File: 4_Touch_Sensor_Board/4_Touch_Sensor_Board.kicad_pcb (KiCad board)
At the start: 2 copper layers, 60 x 31 mm, 21 parts, among them J1 Conn_02x05, U1 TTP224B

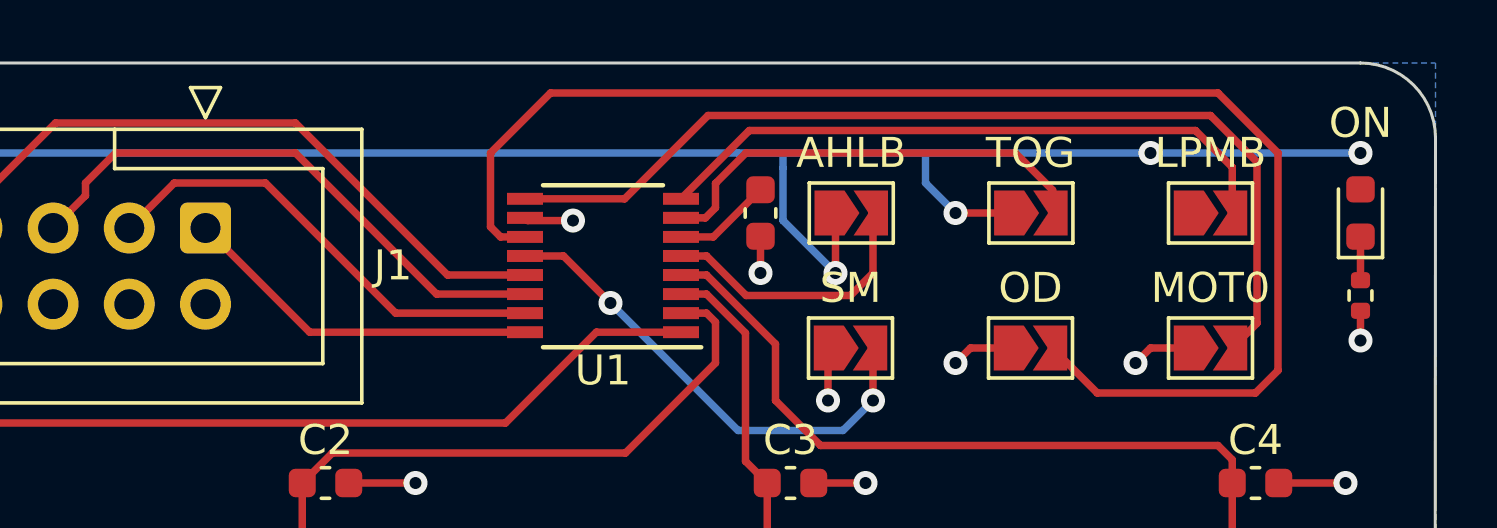
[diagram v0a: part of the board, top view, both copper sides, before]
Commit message: fix board file and add BOM an POS files to JLCPCB
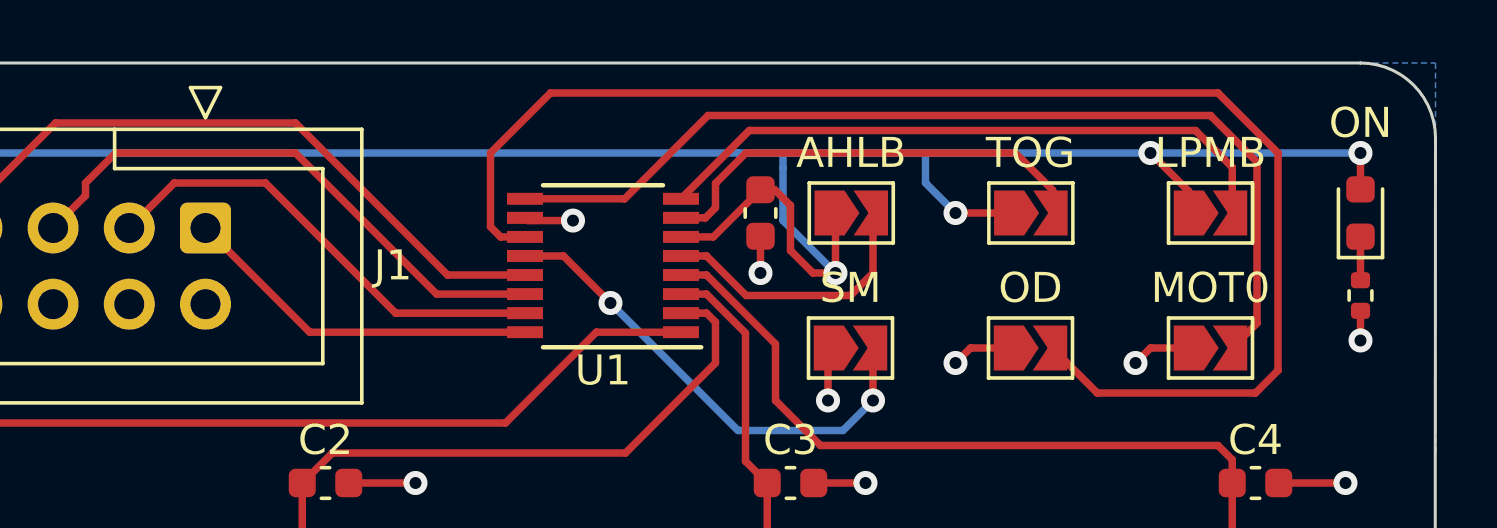
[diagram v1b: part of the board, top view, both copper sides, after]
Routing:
- net +3V3: track 64.0 -> 72.3 mm
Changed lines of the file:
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@@
       (outputformat 1)
       (mirror false)
-      (drillshape 1)
+      (drillshape 0)
       (scaleselection 1)
-      (outputdirectory "")
+      (outputdirectory "Fab/")
     )
   )
@@
     (fp_line (start -1.98 -3.91) (end 4.52 -3.91) (layer "F.Fab") (width 0.1))
     (fp_line (start -1.98 14.07) (end -1.98 7.13) (layer "F.Fab") (width 0.1))
-    (pad "1" thru_hole roundrect locked (at 0 0 270) (size 1.7 1.7) (drill 1) (layers *.Cu *.Mask) (roundrect_rratio 0.147059)
+    (pad "1" thru_hole roundrect locked (at 0 0 270) (size 1.7 1.7) (drill 1) (layers *.Cu *.Mask) (roundrect_rratio 0.1470588235)
       (net 8 "Out_0") (pinfunction "Pin_1") (pintype "passive"))
     (pad "2" thru_hole circle locked (at 2.54 0 270) (size 1.7 1.7) (drill 1) (layers *.Cu *.Mask)
@@
   (segment (start 118 61.25) (end 119.5 62.75) (width 0.25) (layer "F.Cu") (net 5))
   (segment (start 133.225 63.225) (end 133.225 64) (width 0.25) (layer "F.Cu") (net 5))
+  (segment (start 117.975 54.225) (end 118.5 54.75) (width 0.25) (layer "F.Cu") (net 6))
+  (segment (start 119.25 57) (end 120 57) (width 0.25) (layer "F.Cu") (net 6))
+  (segment (start 117.5 54.225) (end 117.975 54.225) (width 0.25) (layer "F.Cu") (net 6))
   (segment (start 120 55.2) (end 119.8 55) (width 0.25) (layer "F.Cu") (net 6))
   (segment (start 120 57) (end 120 55.2) (width 0.25) (layer "F.Cu") (net 6))
+  (segment (start 118.5 56.25) (end 119.25 57) (width 0.25) (layer "F.Cu") (net 6))
   (segment (start 115.9275 55.7975) (end 117.5 54.225) (width 0.25) (layer "F.Cu") (net 6))
   (segment (start 124 55) (end 125.7875 55) (width 0.25) (layer "F.Cu") (net 6))
+  (segment (start 118.5 54.75) (end 118.5 56.25) (width 0.25) (layer "F.Cu") (net 6))
+  (segment (start 137.5 53) (end 137.5 54.2125) (width 0.25) (layer "F.Cu") (net 6))
+  (segment (start 131.775 54.275) (end 131.775 55) (width 0.25) (layer "F.Cu") (net 6))
   (segment (start 114.85 55.7975) (end 115.9275 55.7975) (width 0.25) (layer "F.Cu") (net 6))
+  (segment (start 130.5 53) (end 131.775 54.275) (width 0.25) (layer "F.Cu") (net 6))
   (via (at 120 57) (size 0.8) (drill 0.4) (layers "F.Cu" "B.Cu") (net 6))
   (via (at 137.5 53) (size 0.8) (drill 0.4) (layers "F.Cu" "B.Cu") (net 6))

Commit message: changes to upload
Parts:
- moved REF** 2.15 mm to (128.5, 59.2)
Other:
- board text added: "GitHub: darioGg3/"
